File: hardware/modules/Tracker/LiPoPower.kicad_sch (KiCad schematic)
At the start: 61 parts, among them J701 Battery, J702 Temp&Heater, J703 Ext Switch, J704 LiPo, Q701 Q_NPN_BEC, Q702 Q_PMOS_GSD, SW701 Power Switch, U701 MCP73871-1CC, U702 TPS2116DRL, U703 INA226, U704 INA226, U705 TPS63070RNMR, U706 INA226

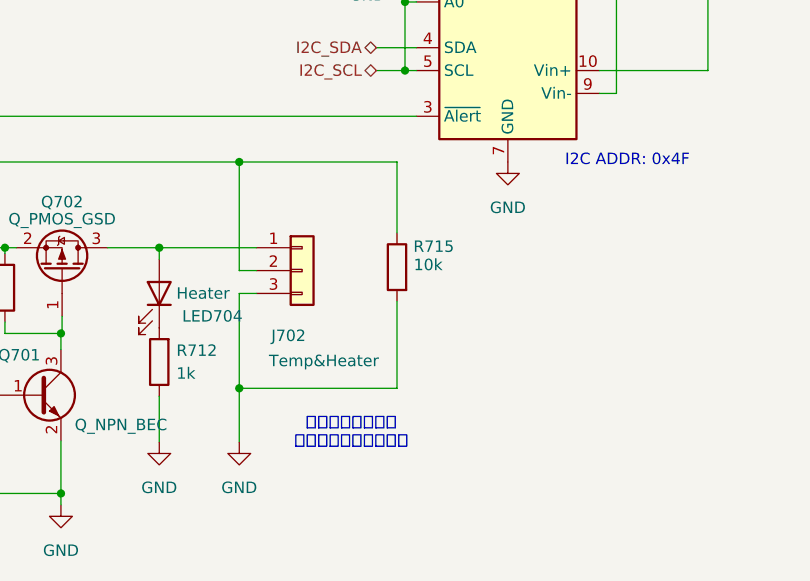
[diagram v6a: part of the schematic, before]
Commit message: 一部Tracker修正（Boot追加、Heater用のピンを追加）
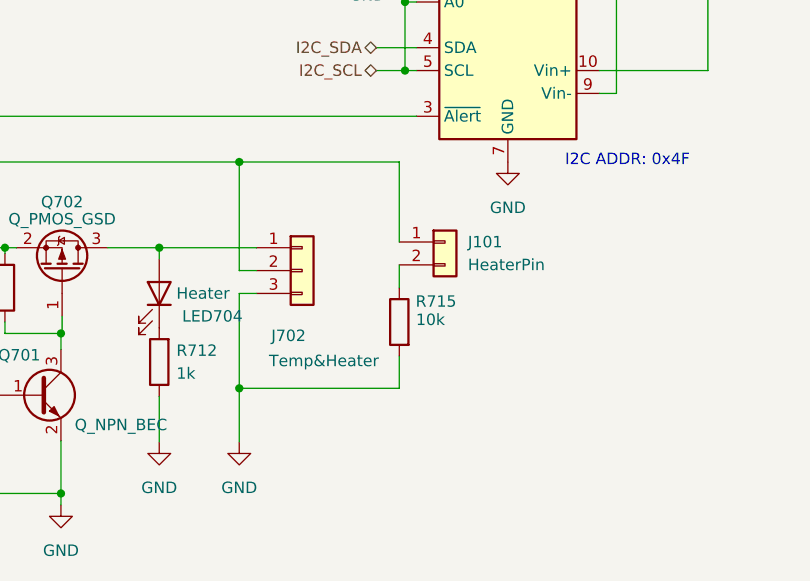
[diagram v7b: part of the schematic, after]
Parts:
- added J101: HeaterPin, Connector_PinHeader_1.27mm:PinHeader_1x02_P1.27mm_Vertical, symbol Connector_Generic:Conn_01x02
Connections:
- net TEMP: now also J101.1 (Pin_1); no longer R715.1
- new net: J101.2 (Pin_2), R715.1
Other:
- note removed: "コネクタあるいは プルダウン抵抗を選択"
- moved on the sheet: R715
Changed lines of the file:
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@@
 	(wire
 		(pts
-			(xy 143.256 152.4) (xy 143.256 160.274)
+			(xy 143.51 152.4) (xy 143.51 161.29)
 		)
 		(stroke
@@
 	(wire
 		(pts
+			(xy 143.51 163.83) (xy 143.51 166.37)
+		)
+		(stroke
+			(width 0)
+			(type default)
+		)
+	)
+	(wire
+		(pts
 			(xy 160.782 119.38) (xy 160.782 117.602)
 		)
@@
 	(wire
 		(pts
-			(xy 125.73 177.546) (xy 143.256 177.546)
+			(xy 125.73 177.546) (xy 143.51 177.546)
 		)
 		(stroke
@@
 	(wire
 		(pts
-			(xy 143.256 177.546) (xy 143.256 167.894)
+			(xy 143.51 177.546) (xy 143.51 173.99)
 		)
 		(stroke
@@
 	(wire
 		(pts
-			(xy 125.73 152.4) (xy 143.256 152.4)
+			(xy 125.73 152.4) (xy 143.51 152.4)
 		)
 		(stroke
@@
 		)
 	)
-	(text "コネクタあるいは\nプルダウン抵抗を選択"
-		(exclude_from_sim no)
-		(at 138.176 182.626 0)
-		(effects
-			(font
-				(size 1.27 1.27)
-			)
-		)
-	)
 	(text "Backup Battery ->"
 		(exclude_from_sim no)
@@
 	(symbol
 		(lib_id "Device:R")
-		(at 143.256 164.084 0)
+		(at 143.51 170.18 0)
 		(mirror y)
 		(unit 1)
@@
 		(dnp no)
 		(property "Reference" "R715"
-			(at 149.606 161.798 0)
+			(at 149.86 167.894 0)
 			(effects
 				(font
@@
 		)
 		(property "Value" "10k"
-			(at 148.336 163.83 0)
+			(at 148.59 169.926 0)
 			(effects
 				(font
@@
 		)
 		(property "Footprint" "Resistor_SMD:R_0402_1005Metric"
-			(at 145.034 164.084 90)
+			(at 145.288 170.18 90)
 			(effects
 				(font
@@
 		)
 		(property "Datasheet" "~"
-			(at 143.256 164.084 0)
+			(at 143.51 170.18 0)
 			(effects
 				(font
@@
 		)
 		(property "Description" ""
-			(at 143.256 164.084 0)
+			(at 143.51 170.18 0)
 			(effects
 				(font
@@
 		)
 		(property "LCSC" "C25744"
-			(at 143.256 164.084 0)
+			(at 143.51 170.18 0)
 			(effects
 				(font
@@
 					(unit 1)
 				)
+			)
+		)
+	)
+	(symbol
+		(lib_id "Connector_Generic:Conn_01x02")
+		(at 148.59 161.29 0)
+		(unit 1)
+		(exclude_from_sim no)
+		(in_bom yes)
+		(on_board yes)
+		(dnp no)
+		(fields_autoplaced yes)
+		(property "Reference" "J101"
+			(at 151.13 161.29 0)
+			(effects
+				(font
+					(size 1.27 1.27)
+				)
+				(justify left)
+			)
+		)
+		(property "Value" "HeaterPin"
+			(at 151.13 163.83 0)
+			(effects
+				(font
+					(size 1.27 1.27)
+				)
+				(justify left)
+			)
+		)
+		(property "Footprint" "Connector_PinHeader_1.27mm:PinHeader_1x02_P1.27mm_Vertical"
+			(at 148.59 161.29 0)
+			(effects
+				(font
+					(size 1.27 1.27)
+				)
+				(hide yes)
+			)
+		)
+		(property "Datasheet" "~"
+			(at 148.59 161.29 0)
+			(effects
+				(font
+					(size 1.27 1.27)
+				)
+				(hide yes)
+			)
+		)
+		(property "Description" ""
+			(at 148.59 161.29 0)
+			(effects
+				(font
+					(size 1.27 1.27)
+				)
+				(hide yes)
+			)
+		)
+		(pin "1"
+		)
+		(pin "2"
+		)
+		(instances
+			(project "Tracker"
+				(path "/485a01ee-6a57-485f-8e4c-0ef4d16d0717/b564a1a6-880f-4f3f-9b5e-b689a4514f2f"
+					(reference "J101")
+					(unit 1)
+				)
